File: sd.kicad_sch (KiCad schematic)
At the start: 47 parts, among them J3 Micro_SD_Card, J4 uSD_edge_contacts, Q1 DMG1032UV, Q2 BSS84, Q3 DMG1032UV, U11 SN74LVC1G14DRL, U12 TS3DDR4000ZBAR, U13 74AUC1G86, U14 GL3224-OIYxx, U15 25LCxxx-MC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

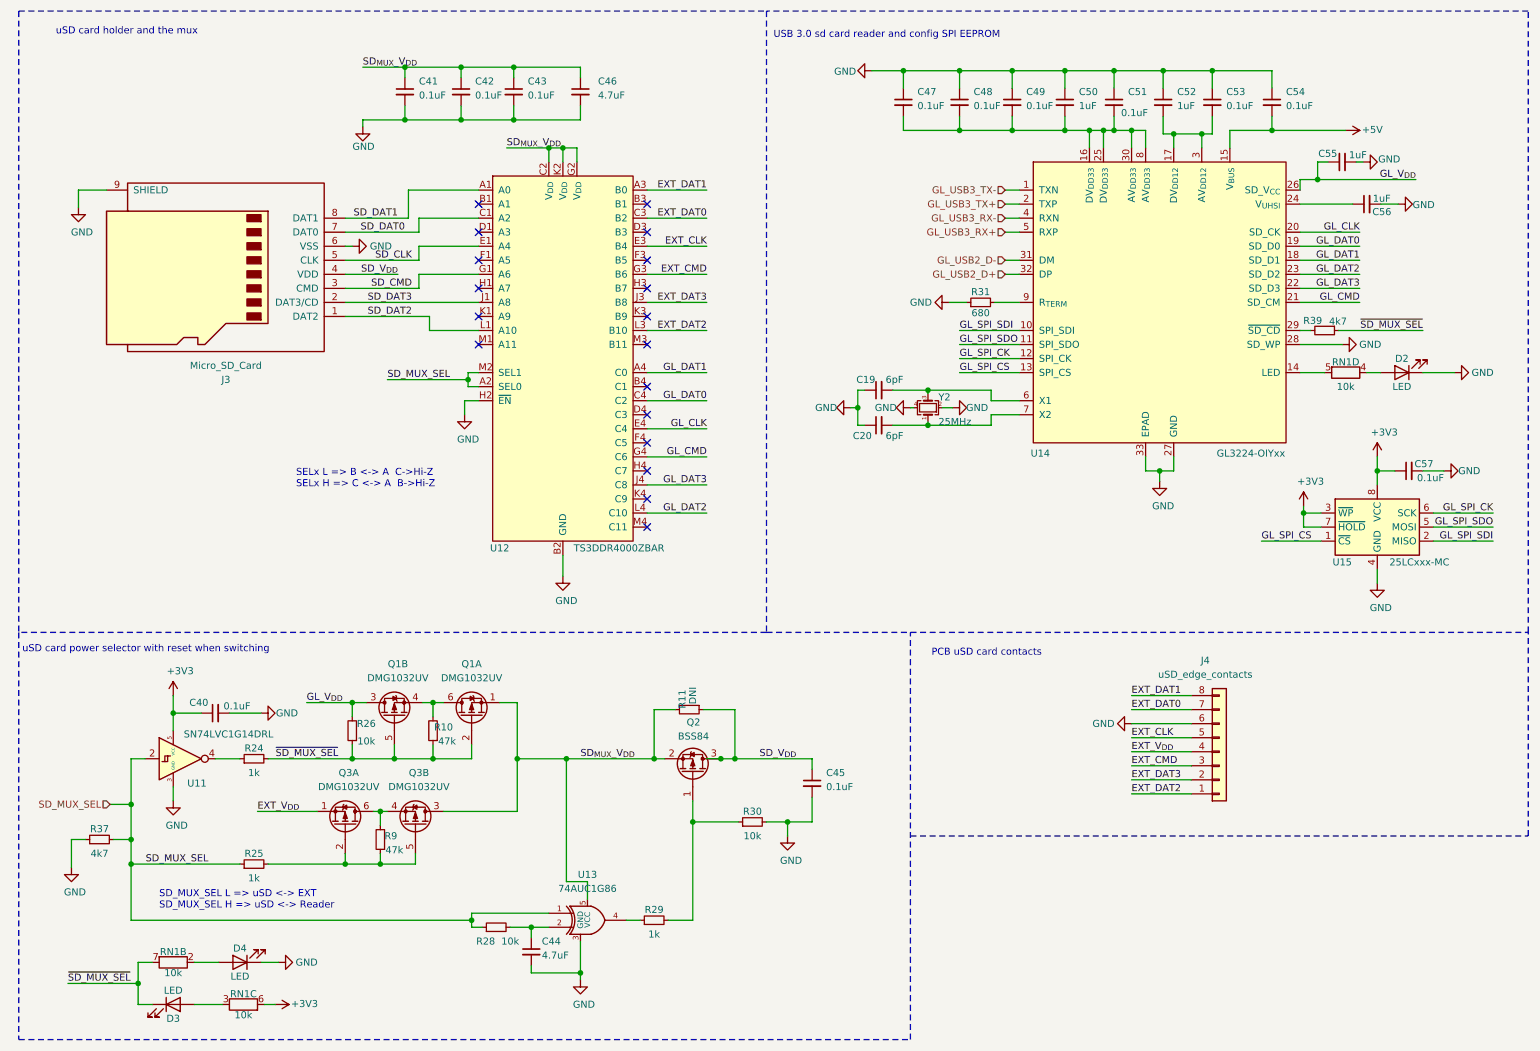
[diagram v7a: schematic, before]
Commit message: sdrewire: pcb v1
Some itra-pair inversions for easier routing.
Fixed crystal pinouts
sd power p-fet changed for smaller package

Signed-off-by: Dominik Sliwa <dominik@sliwa.io>
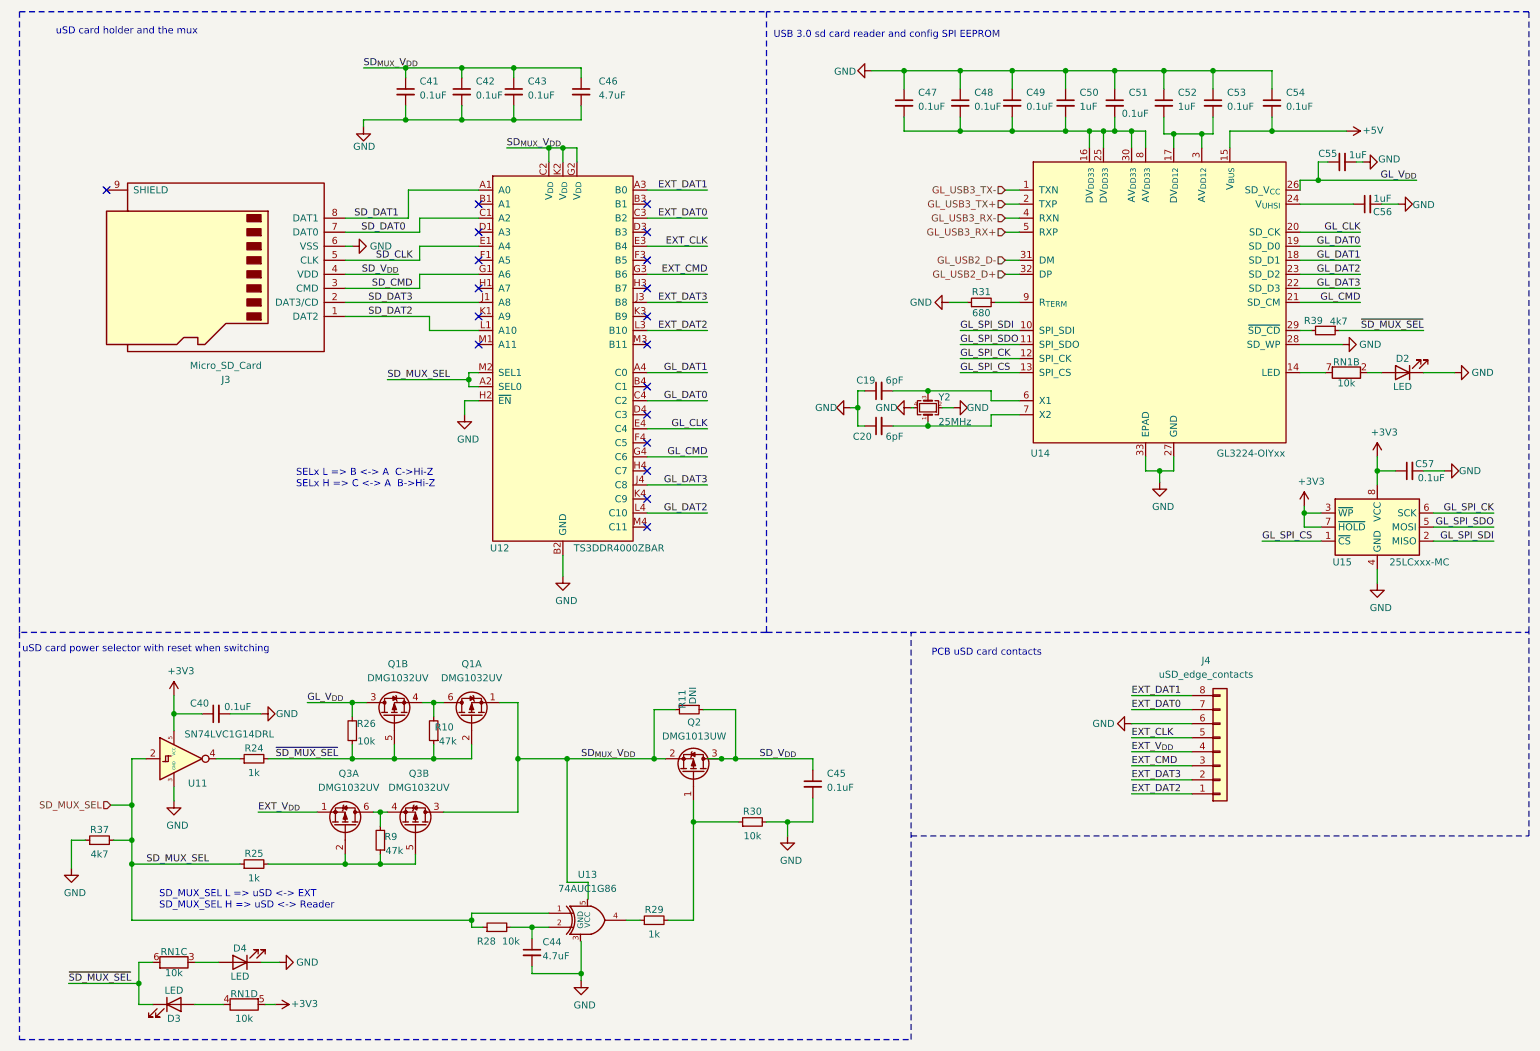
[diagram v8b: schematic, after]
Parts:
- C48: footprint Capacitor_SMD:C_0402_1005Metric -> Capacitor_SMD:C_0201_0603Metric
- Q2: value BSS84 -> DMG1013UW; footprint Package_TO_SOT_SMD:SOT-23 -> Package_TO_SOT_SMD:SOT-323_SC-70
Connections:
- net +3V3: now also RN1.5 (R4.2); no longer RN1.6 (R3.2)
- net GND: no longer J3.9 (SHIELD), U13.3 (GND)
- net SD_{MUX}_V_{DD}: no longer U13.5 (VCC)
- net ~SD_MUX_SEL: now also RN1.6 (R3.2); no longer RN1.7 (R2.2)
- net at U14.14 (LED): now also RN1.7 (R2.2); no longer RN1.5 (R4.2)
- net at D2.2 (A): now also RN1.2 (R2.1); no longer RN1.4 (R4.1)
- net at D3.2 (A): now also RN1.4 (R4.1); no longer RN1.3 (R3.1)
- net at D4.2 (A): now also RN1.3 (R3.1); no longer RN1.2 (R2.1)
- no-connect marks 18 -> 19
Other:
- moved on the sheet: RN1B, RN1C, RN1D
